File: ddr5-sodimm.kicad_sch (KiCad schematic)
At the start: 3 parts, among them J4001 BUS_DDR5_SODIMM_AMPHENOL_1016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

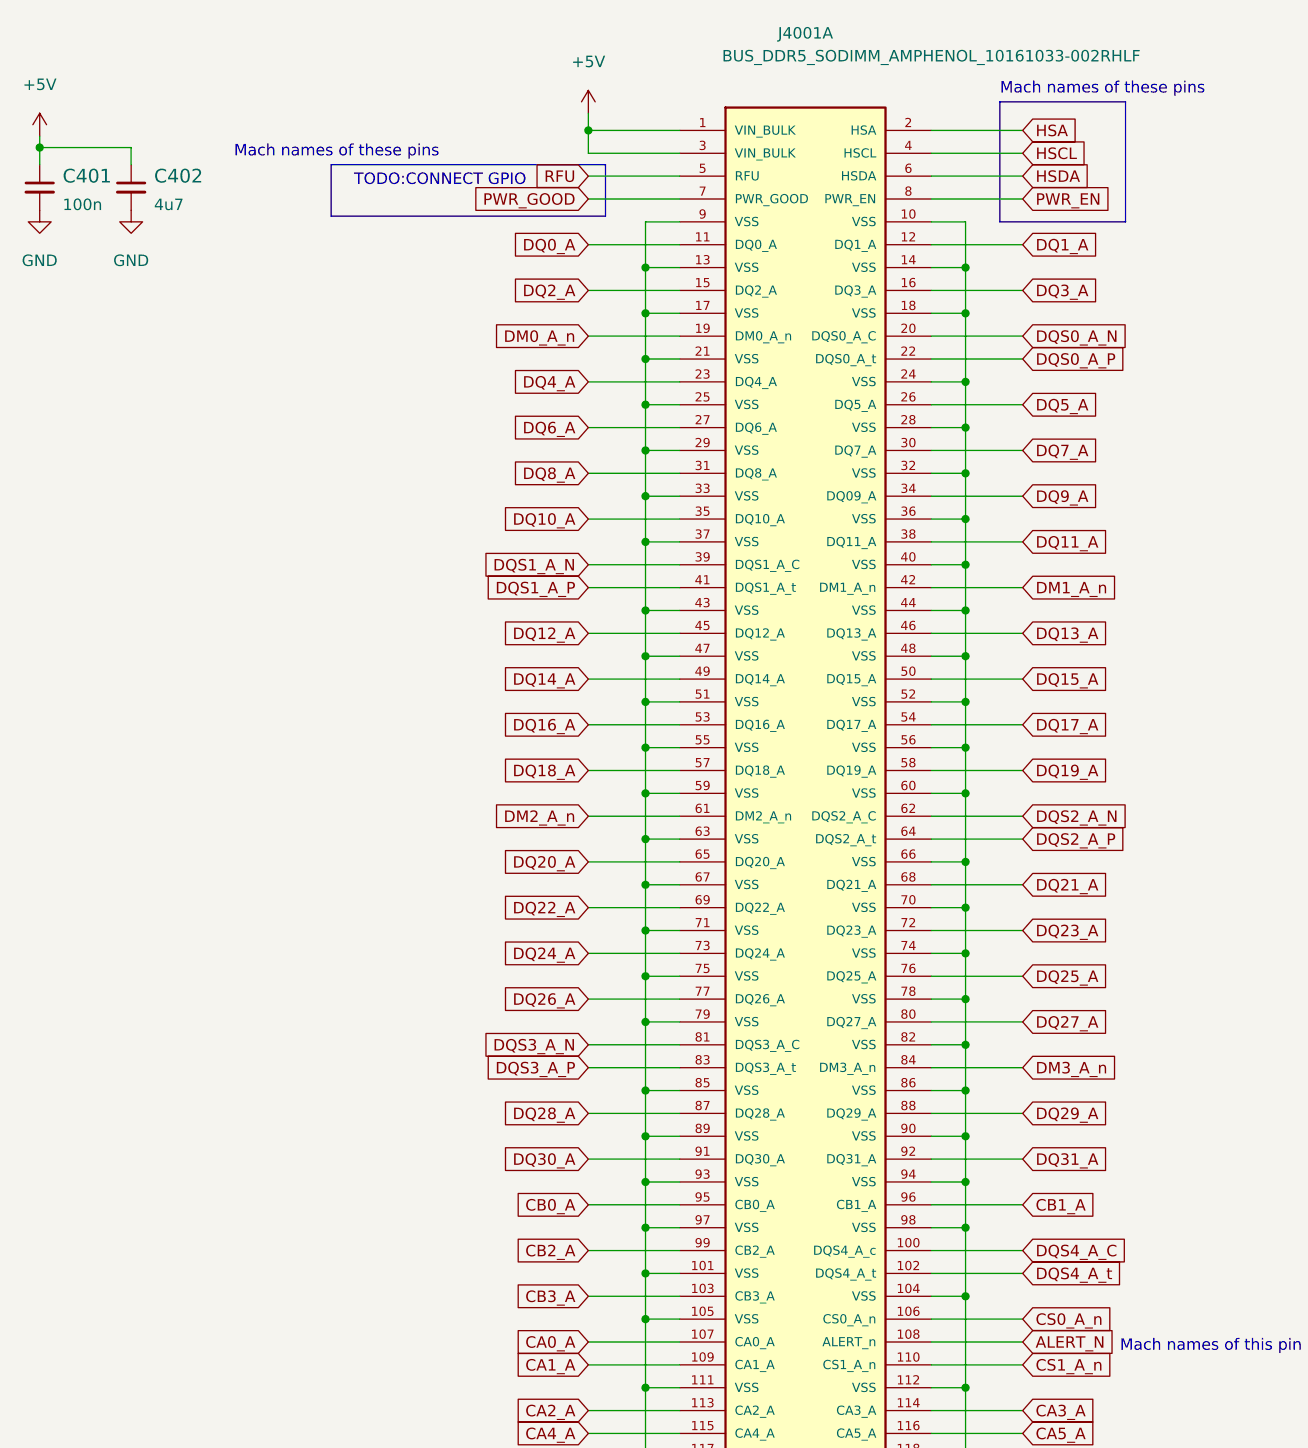
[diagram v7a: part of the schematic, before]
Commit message: Improve DDR assigment, connect ECC to remaining pins, cleanup not used components, continue placement of misc. components
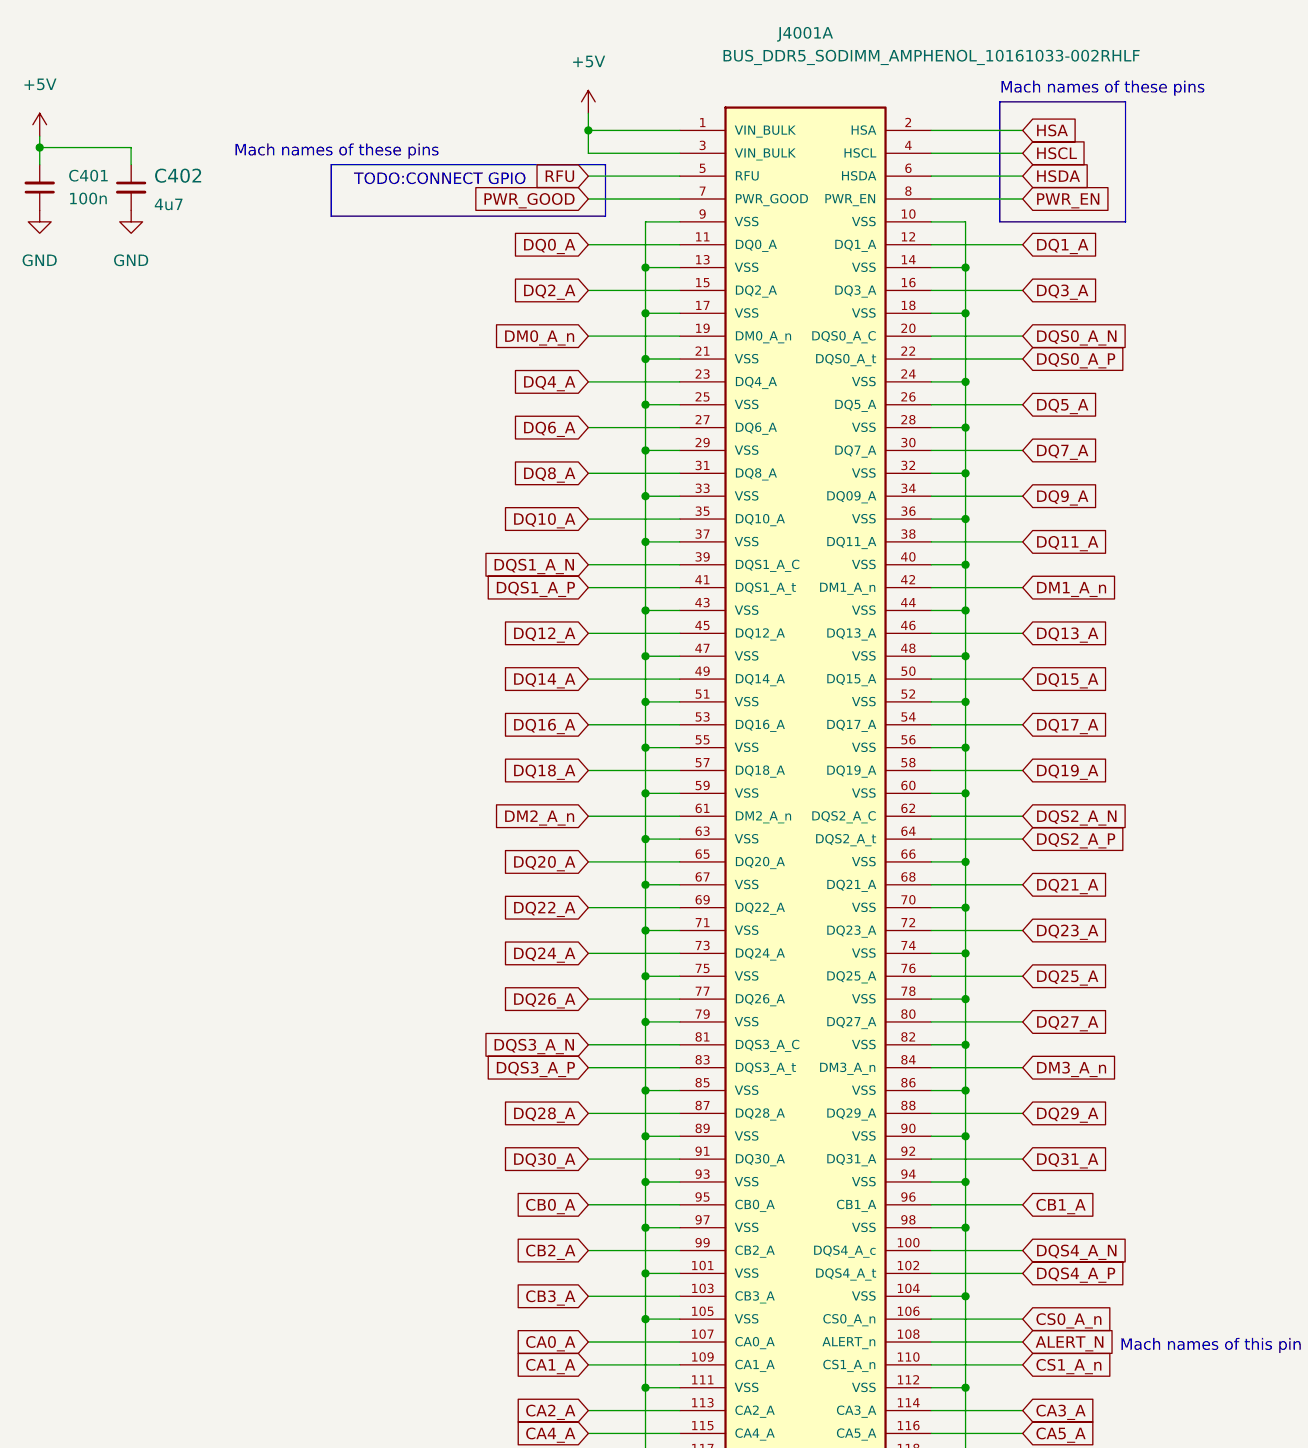
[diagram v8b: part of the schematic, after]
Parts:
- removed C401: C_100n_0201, data-center-rdimm-ddr4-tester-footprints:C_0201, symbol data-center-rdimm-ddr4-tester:C_100n_0201
- added C401: C_100n_0402, antmicro-footprints:C_0402_1005Metric, symbol Capacitors0402:C_100n_0402
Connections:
- net +5V: now also C401.2
- net GND: now also C401.1
- net DQS4_A_C renamed DQS4_A_N
- net DQS4_A_t renamed DQS4_A_P
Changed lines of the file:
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@@
     )
   )
-  (global_label "DQS4_A_C" (shape input) (at 137.795 175.895 0) (fields_autoplaced)
-    (effects (font (size 1.27 1.27)) (justify left))
-    (property "Intersheet References" "${INTERSHEET_REFS}" (id 0) (at 149.4325 175.8156 0)
+  (global_label "DQS4_A_N" (shape input) (at 137.795 175.895 0) (fields_autoplaced)
+    (effects (font (size 1.27 1.27)) (justify left))
+    (property "Intersheet References" "${INTERSHEET_REFS}" (id 0) (at 149.493 175.8156 0)
       (effects (font (size 1.27 1.27)) (justify left) hide)
     )
@@
     )
   )
-  (global_label "DQS4_A_t" (shape input) (at 137.795 178.435 0) (fields_autoplaced)
-    (effects (font (size 1.27 1.27)) (justify left))
-    (property "Intersheet References" "${INTERSHEET_REFS}" (id 0) (at 148.8882 178.3556 0)
+  (global_label "DQS4_A_P" (shape input) (at 137.795 178.435 0) (fields_autoplaced)
+    (effects (font (size 1.27 1.27)) (justify left))
+    (property "Intersheet References" "${INTERSHEET_REFS}" (id 0) (at 149.4325 178.3556 0)
       (effects (font (size 1.27 1.27)) (justify left) hide)
     )
@@
     )
     (pin "1")
-  )
-  (symbol (lib_id "data-center-rdimm-ddr4-tester:C_100n_0201") (at 28.575 55.245 270) (unit 1)
-    (in_bom yes) (on_board yes) (fields_autoplaced)
-    (property "Reference" "C401" (id 0) (at 31.115 56.5213 90)
-      (effects (font (size 1.524 1.524)) (justify left))
-    )
-    (property "Value" "C_100n_0201" (id 1) (at 18.415 75.565 0)
-      (effects (font (size 1.27 1.27) (thickness 0.15)) (justify left bottom) hide)
-    )
-    (property "Footprint" "data-center-rdimm-ddr4-tester-footprints:C_0201" (id 2) (at 15.875 75.565 0)
-      (effects (font (size 1.27 1.27) (thickness 0.15)) (justify left bottom) hide)
-    )
-    (property "Datasheet" " " (id 3) (at 13.335 75.565 0)
-      (effects (font (size 1.27 1.27) (thickness 0.15)) (justify left bottom) hide)
-    )
-    (property "Manufacturer" "Yaego" (id 4) (at 8.255 75.565 0)
-      (effects (font (size 1.27 1.27) (thickness 0.15)) (justify left bottom) hide)
-    )
-    (property "MPN" "CC0201KRX6S5BB104" (id 5) (at 10.795 75.565 0)
-      (effects (font (size 1.27 1.27) (thickness 0.15)) (justify left bottom) hide)
-    )
-    (property "Val" "100n" (id 6) (at 31.115 59.6962 90)
-      (effects (font (size 1.27 1.27) (thickness 0.15)) (justify left))
-    )
-    (property "License" "Apache-2.0" (id 7) (at 5.715 75.565 0)
-      (effects (font (size 1.27 1.27) (thickness 0.15)) (justify left bottom) hide)
-    )
-    (property "Author" "Antmicro" (id 8) (at 3.175 75.565 0)
-      (effects (font (size 1.27 1.27) (thickness 0.15)) (justify left bottom) hide)
-    )
-    (property "Voltage" "" (id 9) (at 0.635 75.565 0)
-      (effects (font (size 1.27 1.27)) (justify left bottom) hide)
-    )
-    (property "Dielectric" "" (id 10) (at -1.905 75.565 0)
-      (effects (font (size 1.27 1.27)) (justify left bottom) hide)
-    )
-    (pin "1")
-    (pin "2")
   )
   (symbol (lib_name "BUS_DDR5_SODIMM_AMPHENOL_10161033-002RHLF_1") (lib_id "antmicroMemoryConnectorsPCCardSockets:BUS_DDR5_SODIMM_AMPHENOL_10161033-002RHLF") (at 294.64 130.175 0) (unit 2)
@@
     (pin "262")
   )
+  (symbol (lib_id "Capacitors0402:C_100n_0402") (at 28.575 60.325 90) (unit 1)
+    (in_bom yes) (on_board yes) (fields_autoplaced)
+    (property "Reference" "C401" (id 0) (at 31.75 56.5085 90)
+      (effects (font (size 1.27 1.27) (thickness 0.15)) (justify right))
+    )
+    (property "Value" "C_100n_0402" (id 1) (at 38.735 40.005 0)
+      (effects (font (size 1.27 1.27) (thickness 0.15)) (justify left bottom) hide)
+    )
+    (property "Footprint" "antmicro-footprints:C_0402_1005Metric" (id 2) (at 41.275 40.005 0)
+      (effects (font (size 1.27 1.27) (thickness 0.15)) (justify left bottom) hide)
+    )
+    (property "Datasheet" "https://www.murata.com/products/productdetail?partno=GRM155R61H104KE14%23" (id 3) (at 43.815 40.005 0)
+      (effects (font (size 1.27 1.27) (thickness 0.15)) (justify left bottom) hide)
+    )
+    (property "MPN" "GRM155R61H104KE14D" (id 4) (at 46.355 40.005 0)
+      (effects (font (size 1.27 1.27) (thickness 0.15)) (justify left bottom) hide)
+    )
+    (property "Manufacturer" "Murata" (id 5) (at 48.895 40.005 0)
+      (effects (font (size 1.27 1.27) (thickness 0.15)) (justify left bottom) hide)
+    )
+    (property "License" "Apache-2.0" (id 6) (at 51.435 40.005 0)
+      (effects (font (size 1.27 1.27) (thickness 0.15)) (justify left bottom) hide)
+    )
+    (property "Author" "Antmicro" (id 7) (at 53.975 40.005 0)
+      (effects (font (size 1.27 1.27) (thickness 0.15)) (justify left bottom) hide)
+    )
+    (property "Val" "100n" (id 8) (at 31.75 59.0485 90)
+      (effects (font (size 1.27 1.27) (thickness 0.15)) (justify right))
+    )
+    (property "Voltage" "50V" (id 9) (at 56.515 40.005 0)
+      (effects (font (size 1.27 1.27)) (justify left bottom) hide)
+    )
+    (property "Dielectric" "X5R" (id 10) (at 59.055 40.005 0)
+      (effects (font (size 1.27 1.27)) (justify left bottom) hide)
+    )
+    (pin "1")
+    (pin "2")
+  )
   (symbol (lib_id "antmicroMemoryConnectorsPCCardSockets:BUS_DDR5_SODIMM_AMPHENOL_10161033-002RHLF") (at 113.665 130.175 0) (unit 1)
